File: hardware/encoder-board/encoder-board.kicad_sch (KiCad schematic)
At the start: 26 parts, among them J1 Conn_01x04, U1 ITR1204SR10A_TR(BY), U2 ITR1204SR10A_TR(BY), U3 LM2903

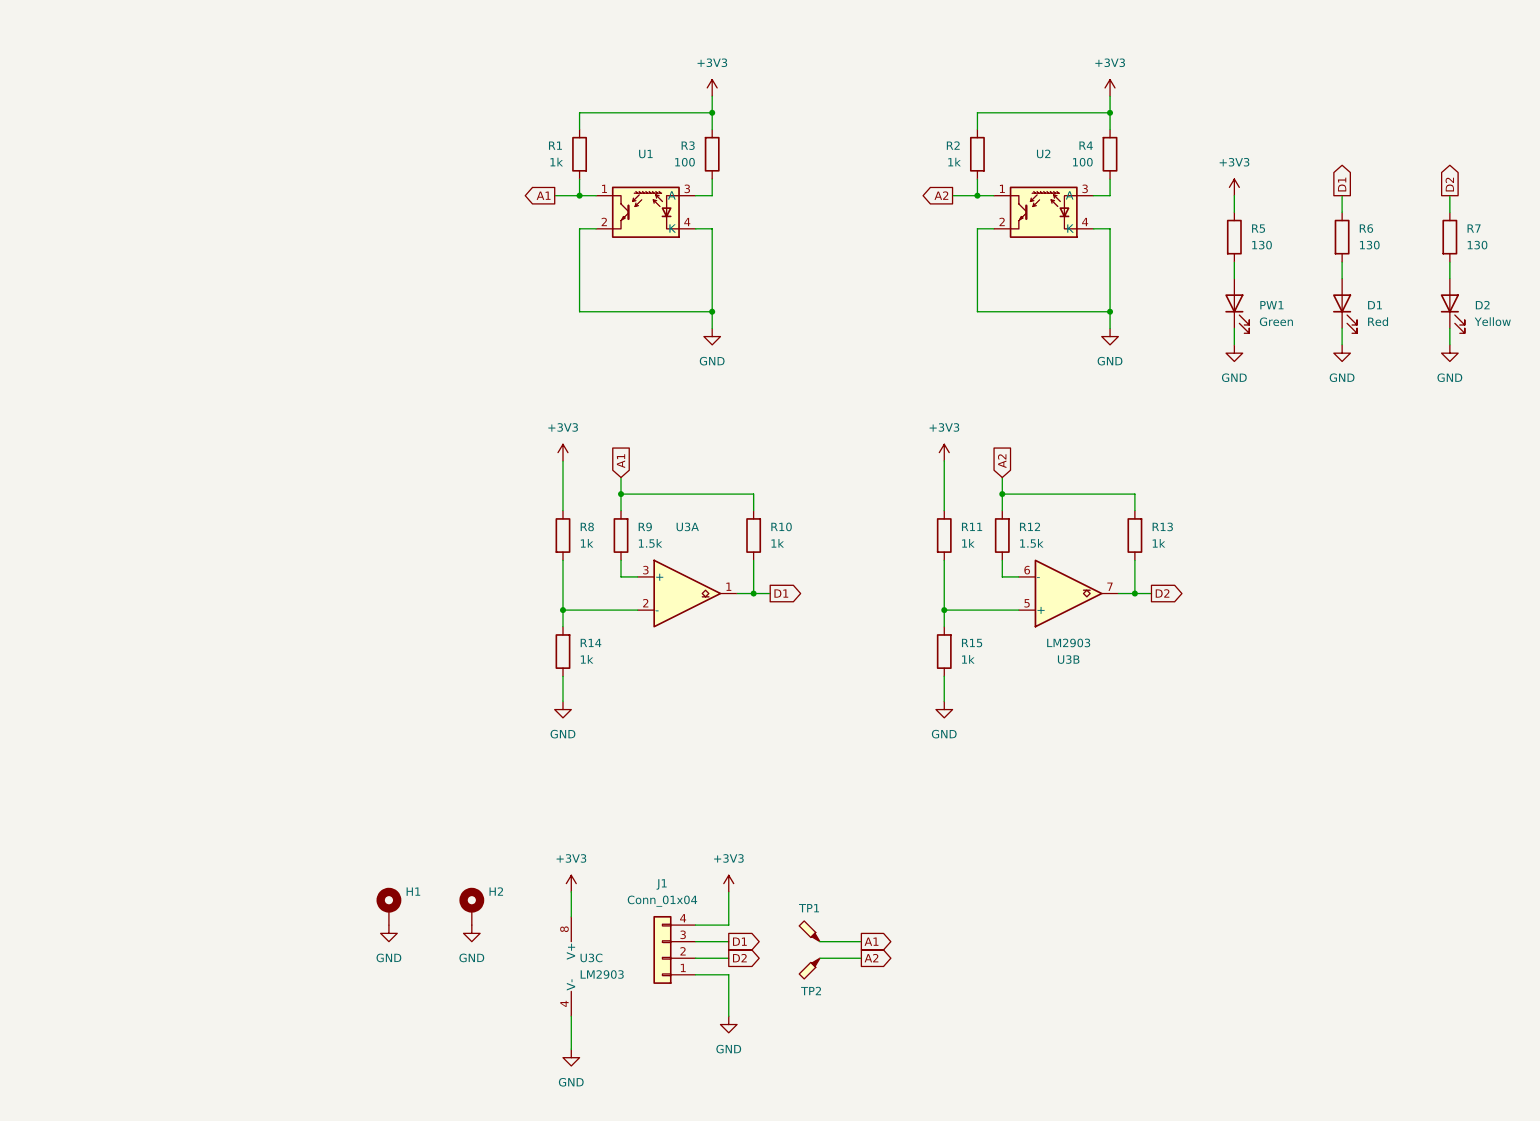
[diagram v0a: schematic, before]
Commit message: fix encoder schematics. Prepare to redo pcb.
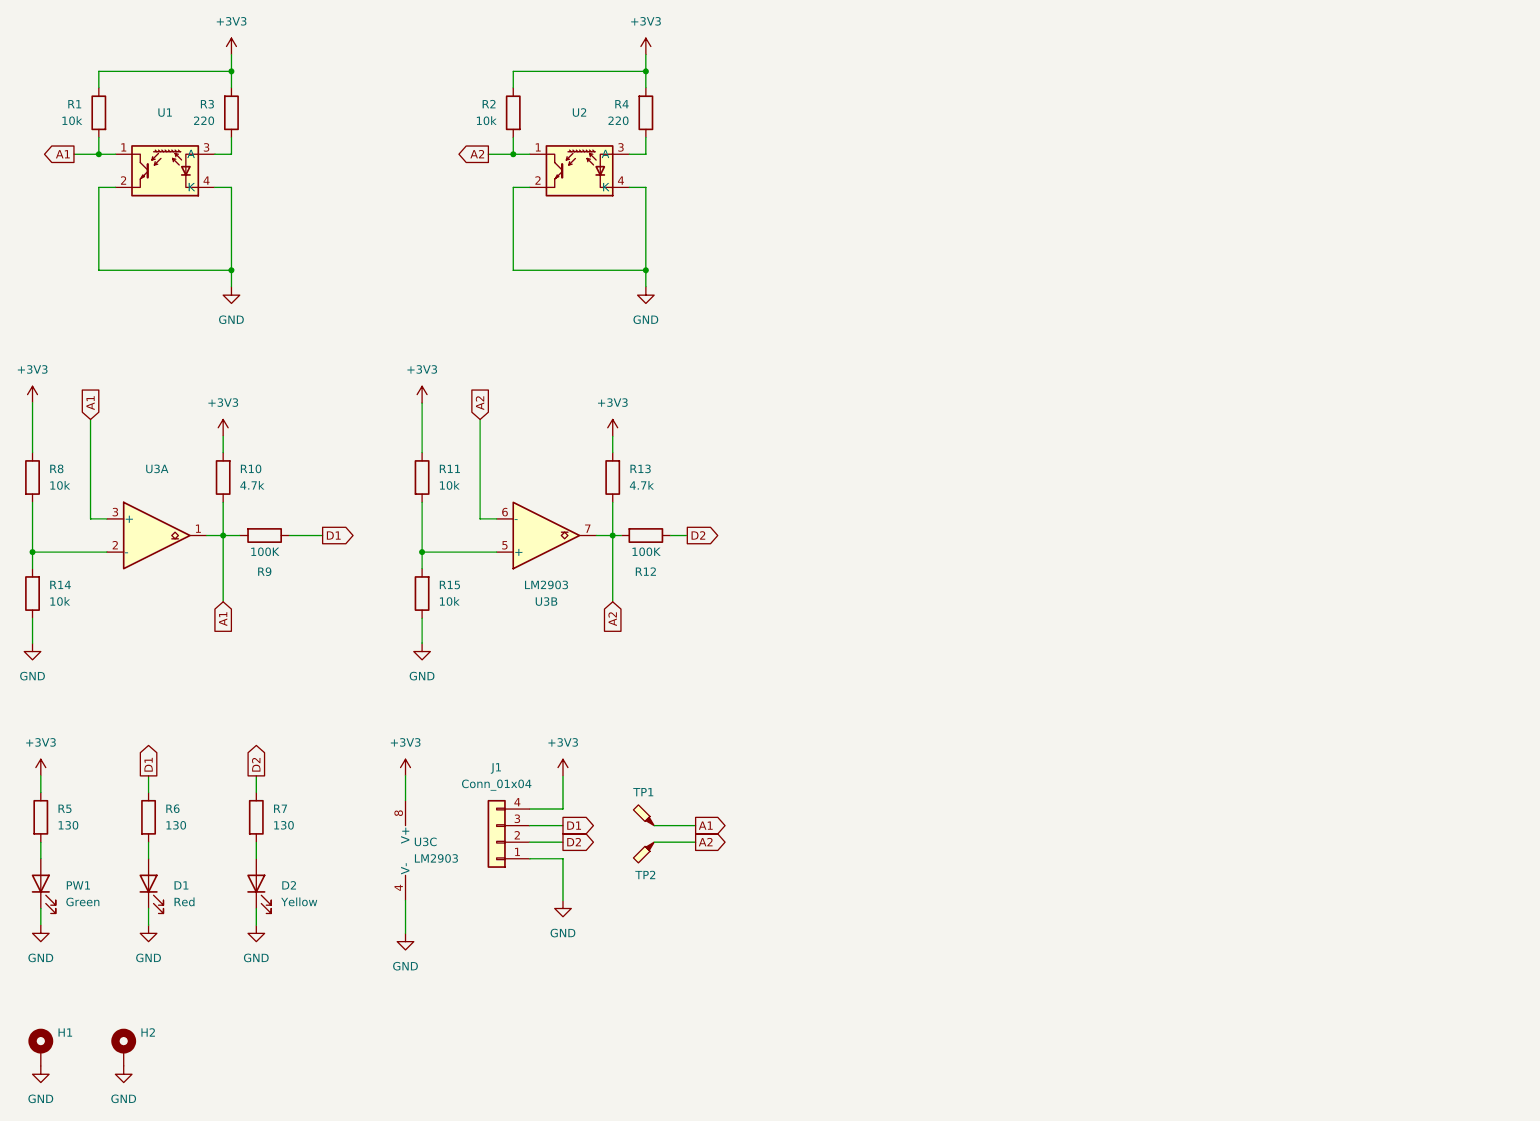
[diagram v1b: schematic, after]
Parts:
- R1, R11, R14, R15, R2, R8: value 1k -> 10k
- R10, R13: value 1k -> 4.7k
- R12, R9: value 1.5k -> 100K; LCSC C114668 -> C22548
- R3, R4: value 100 -> 220
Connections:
- net +3V3: now also R10.2, R13.2
- net A1: now also R10.1, U3.1, U3.3 (+); no longer R10.2
- net A2: now also R13.1, U3.6 (-), U3.7; no longer R13.2
- net D1: now also R9.1; no longer R10.1, U3.1
- net D2: now also R12.1; no longer R13.1, U3.7
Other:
- moved on the sheet: D1, D2, H1, H2, J1, PW1, R1, R10, R11, R13, R14, R15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
